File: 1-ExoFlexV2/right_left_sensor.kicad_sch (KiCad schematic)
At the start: 20 parts, among them U30 SN74LVC3G14DCUT_V2, U31 SN74LVC3G14DCUT_V2, U32 SN74LVC1G08DBVR, U33 SN74LVC3G14DCUT_V2, U34 SN74LVC3G14DCUT_V2, U35 SN74LVC1G08DBVR, U36 SN74LVC1G32DBVR

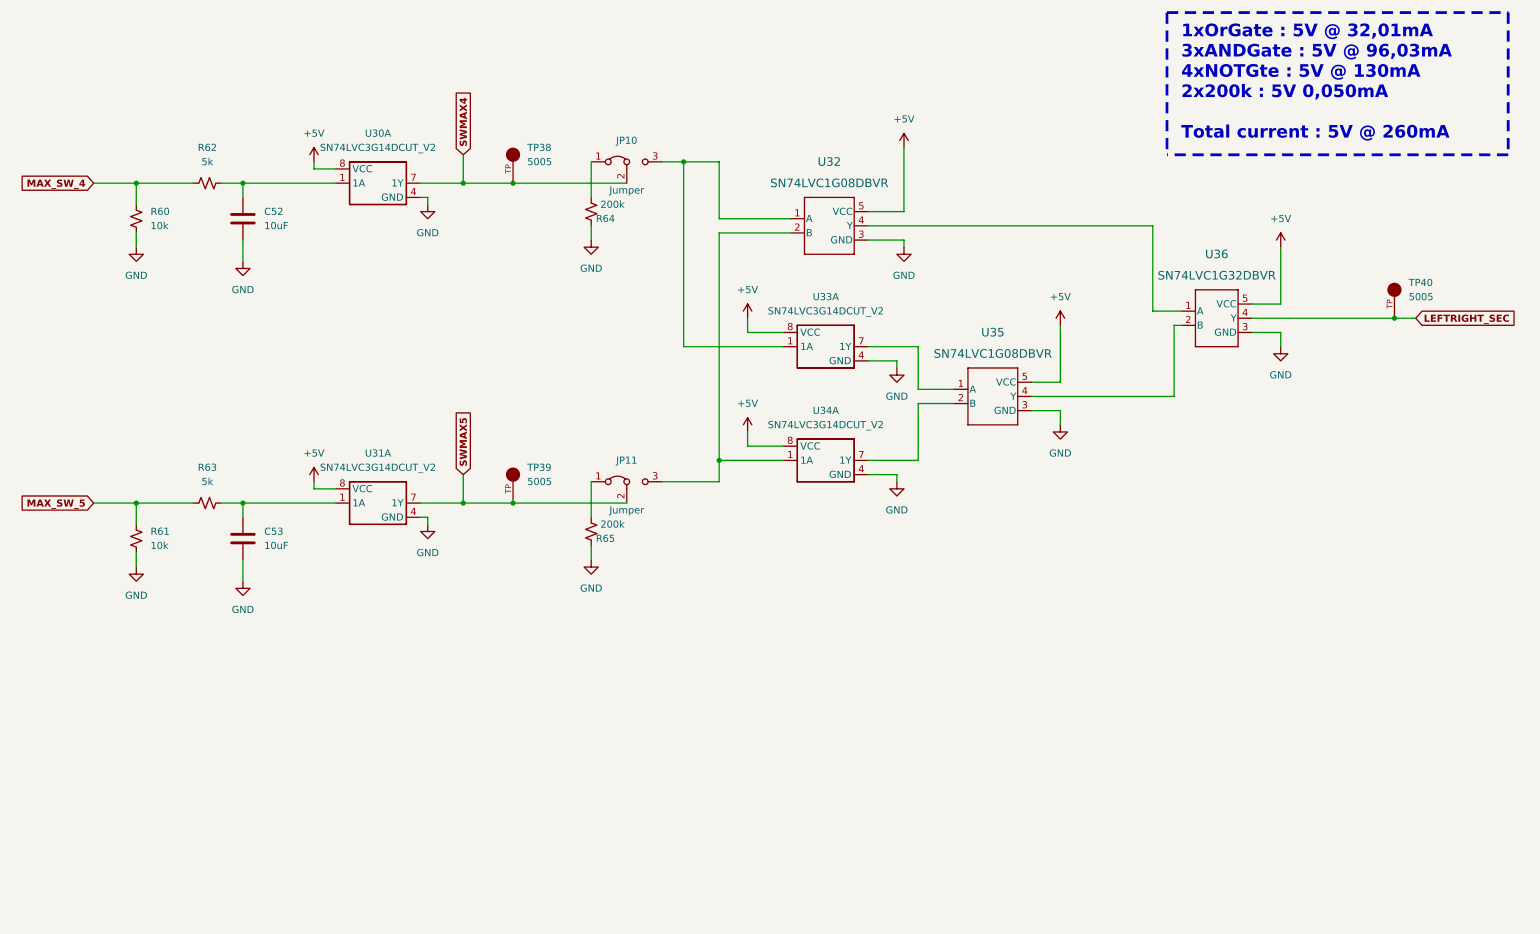
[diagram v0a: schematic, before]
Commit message: Chokes et RC
- Ajout des RF chokes
- Changement des résistance pour 0805
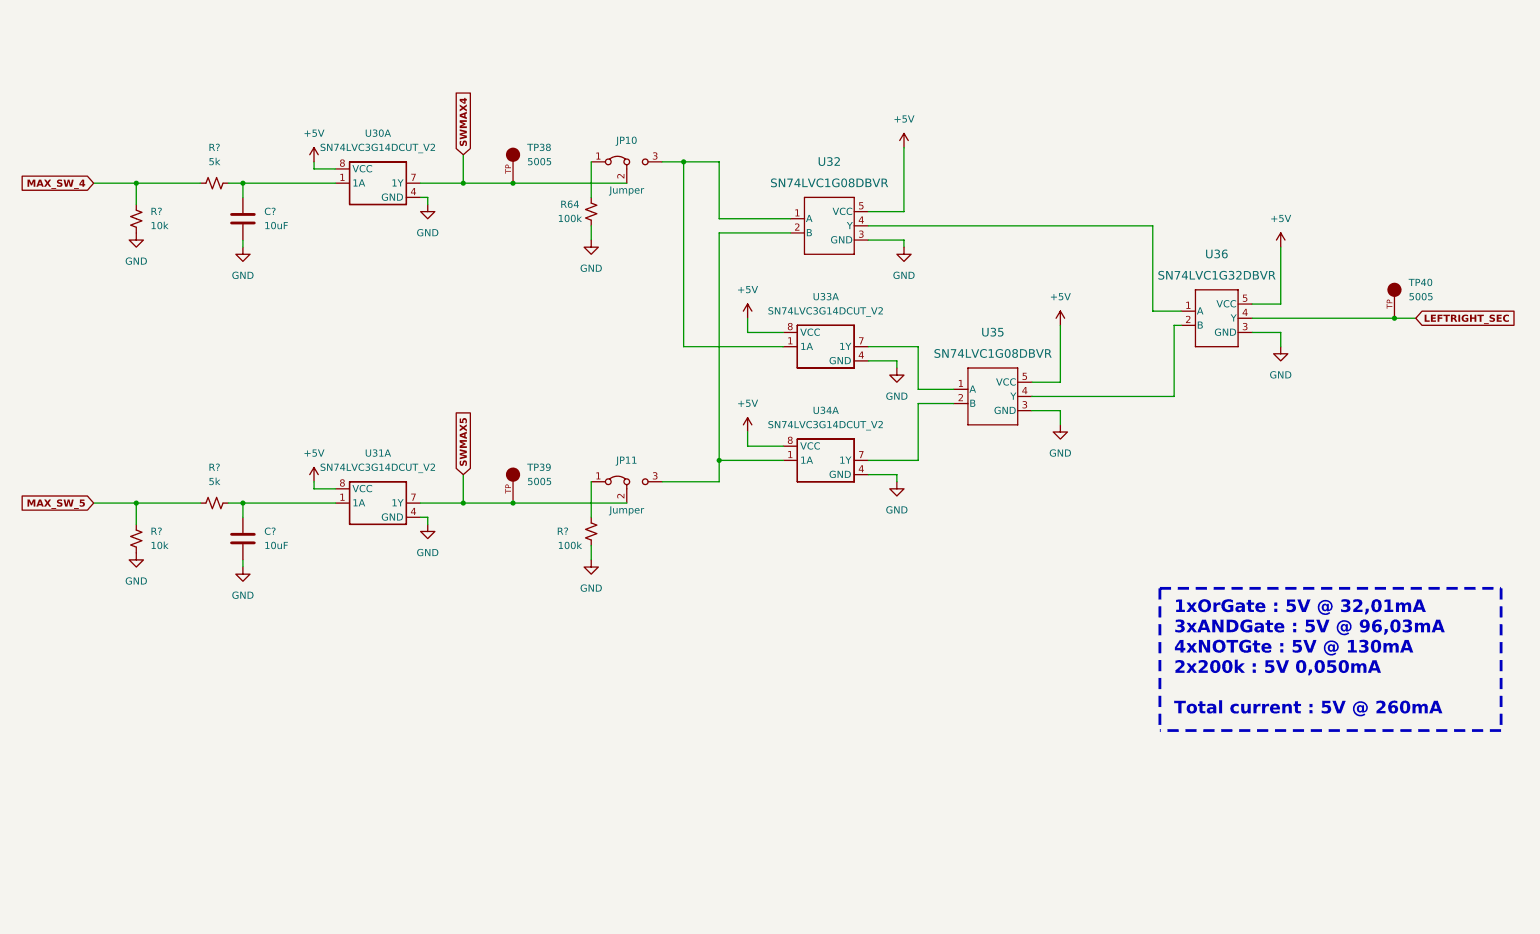
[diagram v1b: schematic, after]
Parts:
- removed C52, C53: 10uF, Capacitor_SMD:C_0603_1608Metric, symbol Device:C
- removed R60, R61: 10k, Resistor_SMD:R_0603_1608Metric, symbol Device:R_Small_US
- removed R62, R63: 5k, Resistor_SMD:R_0603_1608Metric, symbol Device:R_Small_US
- removed R65: 200k, Resistor_SMD:R_0603_1608Metric, symbol Device:R_Small_US
- added C? (x2): 10uF, Capacitor_SMD:C_0805_2012Metric, symbol Device:C
- added R?: 100k, Resistor_SMD:R_0805_2012Metric, symbol Device:R_Small_US
- added R? (x2): 10k, Resistor_SMD:R_0805_2012Metric, symbol Device:R_Small_US
- added R? (x2): 5k, Resistor_SMD:R_0805_2012Metric, symbol Device:R_Small_US
- R64: value 200k -> 100k; footprint Resistor_SMD:R_0603_1608Metric -> Resistor_SMD:R_0805_2012Metric
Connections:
- net GND: now also C?.2, C?.2, R?.2, R?.2, R?.2
- net MAX_SW_4: now also R?.1, R?.1
- net MAX_SW_5: now also R?.1, R?.1
- net at U30.1 (1A): now also C?.1, R?.2
- net at U31.1 (1A): now also C?.1, R?.2
- net at JP11.1 (A): now also R?.1

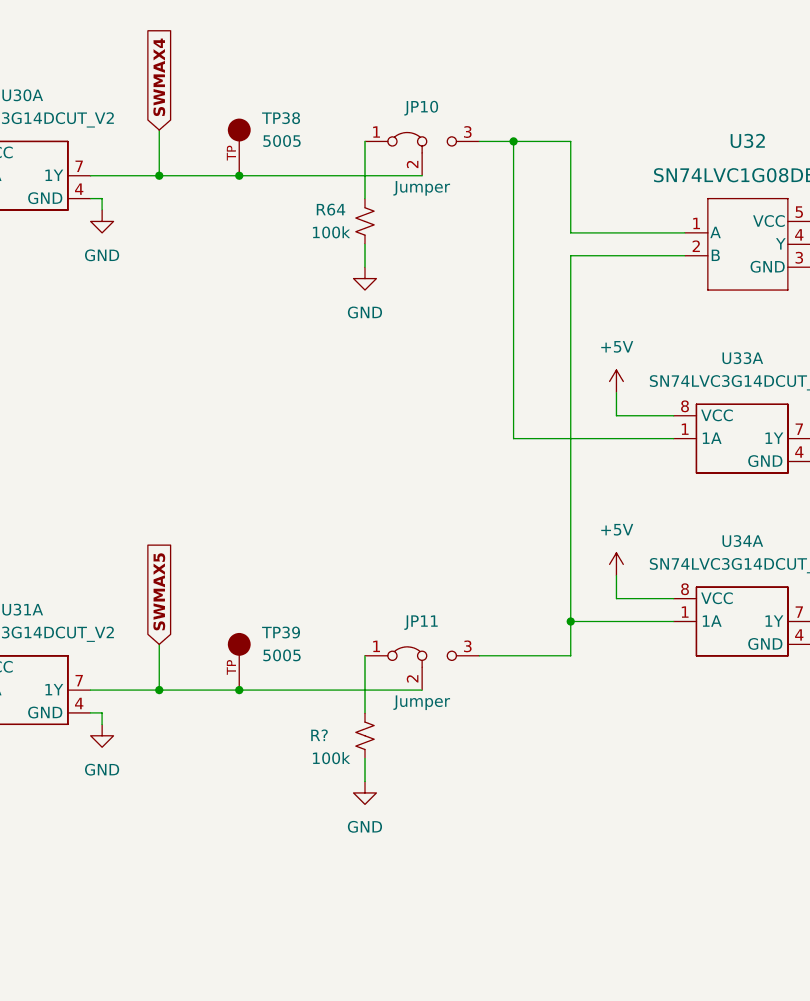
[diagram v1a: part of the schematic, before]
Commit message: Trimmer et jumper
-Changement de symbole de jumper
-Ajout des des trimmer aux endroits nécessaires
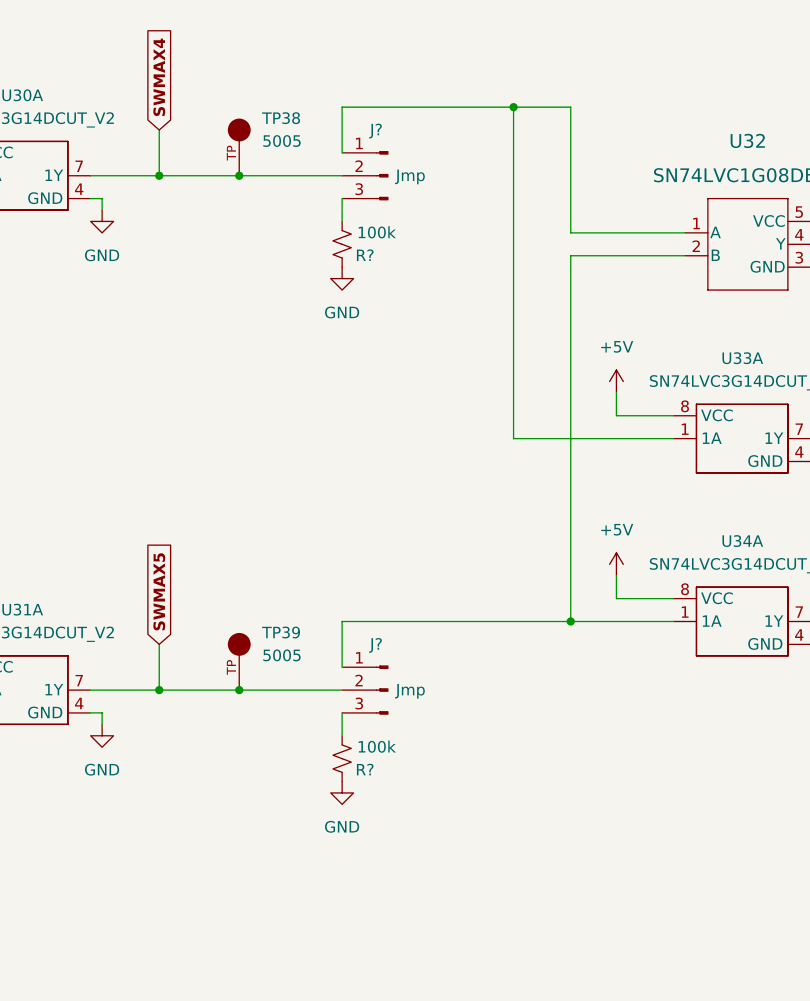
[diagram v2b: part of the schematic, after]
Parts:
- removed JP10, JP11: Jumper, Connector_PinHeader_2.54mm:PinHeader_1x03_P2.54mm_Vertical, symbol Jumper:Jumper_3_Bridged12
- removed R64, R?: 100k, Resistor_SMD:R_0805_2012Metric, symbol Device:R_Small_US
- added J? (x2): Jmp, symbol Connector:Conn_01x03_Male
- added R? (x2): 100k, Resistor_SMD:R_0805_2012Metric, symbol Device:R_Small_US
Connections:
- net GND: now also R?.2, R?.2
- net SWMAX4: now also J?.2 (Pin_2)
- net SWMAX5: now also J?.2 (Pin_2)
- net at U32.1 (A), U33.1 (1A): now also J?.1 (Pin_1)
- net at U32.2 (B), U34.1 (1A): now also J?.1 (Pin_1)
- new net: J?.3 (Pin_3), R?.1 (x2)
